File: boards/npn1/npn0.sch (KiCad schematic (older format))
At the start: 16 parts, among them P1 CONN_01X02, P2 CONN_01X02, P3 CONN_01X02, Q1 TIP122, Q2 BC817-40, U1 LM324N, U2 TL431_SOT23-3

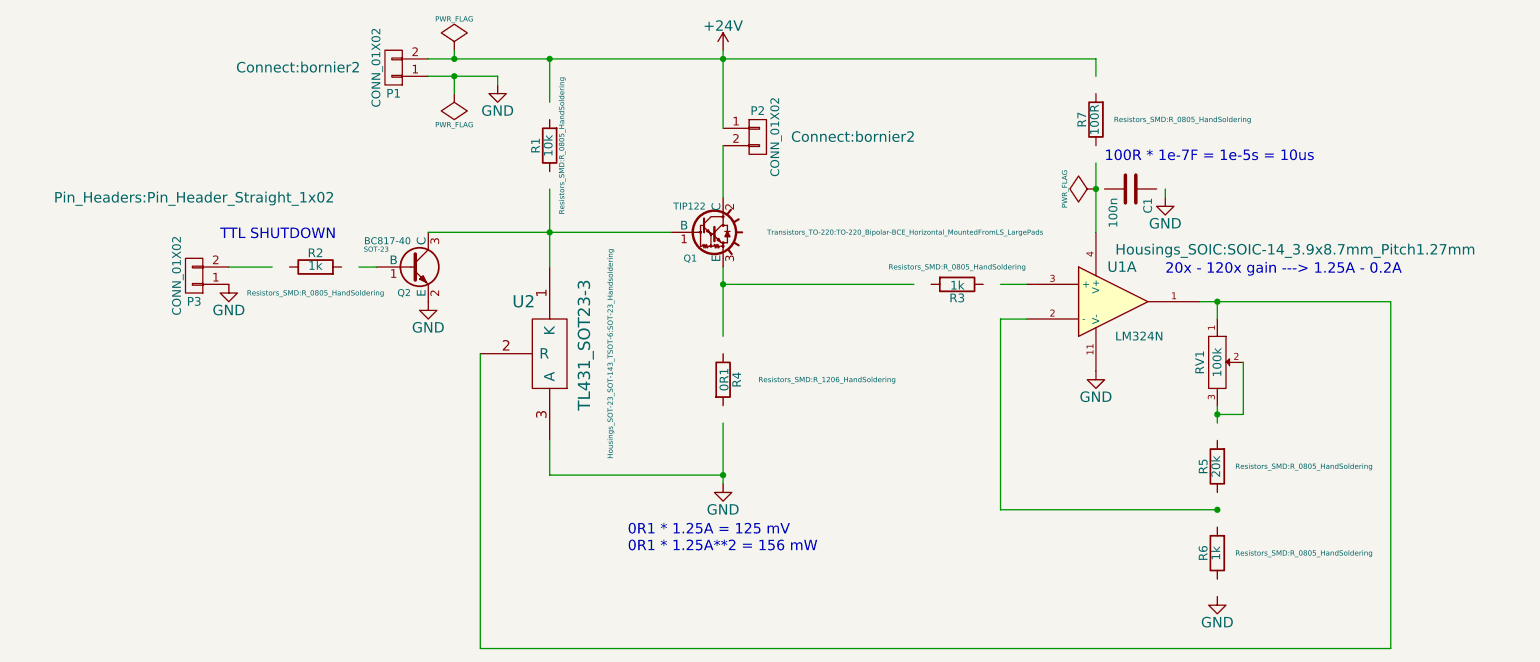
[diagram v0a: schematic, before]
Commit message: designing NPN and opAmp based regulators
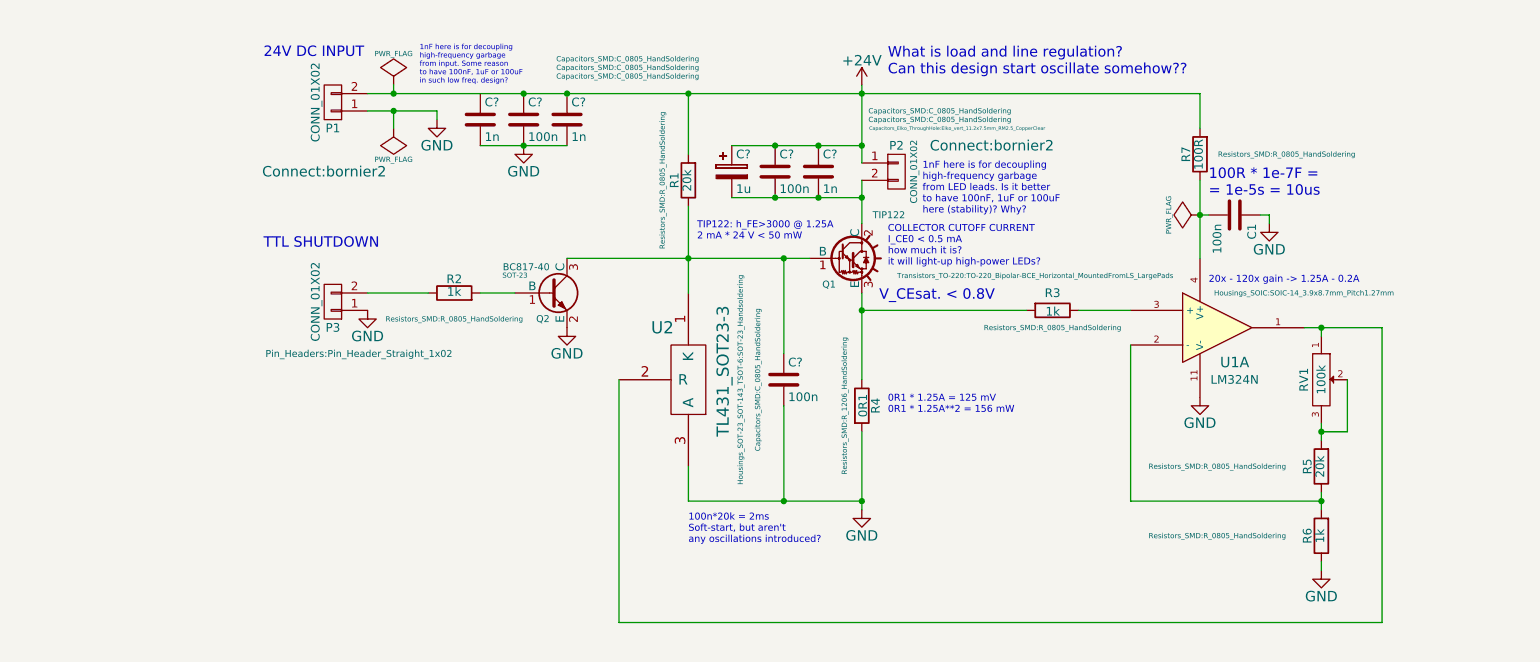
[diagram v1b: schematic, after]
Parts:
- added C? (x3): 1n, Capacitors_SMD:C_0805_HandSoldering, symbol C
- added C? (x3): 100n, Capacitors_SMD:C_0805_HandSoldering, symbol C
- added C?: 1u, Capacitors_Elko_ThroughHole:Elko_vert_11.2x7.5mm_RM2.5_CopperClear, symbol CP
- R1: value 10k -> 20k
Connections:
- wire segments 32 -> 41
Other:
- note added: "100R * 1e-7F =\n= 1e-5s = 10us"
- note added: "100n*20k = 2ms\nSoft-start, but aren't\nany oscillations introduced?"
- note added: "1nF here is for decoupling\nhigh-frequency garbage\nfrom LED leads. Is it better\nto have 100nF, 1uF or 100uF\nhere (stability)? Why?"
- note added: "1nF here is for decoupling\nhigh-frequency garbage\nfrom input. Some reason\nto have 100nF, 1uF or 100uF\nin such low freq. design?"
- note added: "20x - 120x gain -> 1.25A - 0.2A"
- note added: "24V DC INPUT"
- note added: "COLLECTOR CUTOFF CURRENT\nI_CE0 < 0.5 mA\nhow much it is?\nit will light-up high-power LEDs?"
- note added: "TIP122: h_FE>3000 @ 1.25A\n2 mA * 24 V < 50 mW"
- note added: "V_CEsat. < 0.8V"
- note added: "What is load and line regulation?\nCan this design start oscillate somehow??"
- note removed: "100R * 1e-7F = 1e-5s = 10us"
- note removed: "20x - 120x gain ---> 1.25A - 0.2A"
- moved on the sheet: C1, P1, P2, P3, Q1, Q2, R1, R2, R3, R4, R5, R6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
